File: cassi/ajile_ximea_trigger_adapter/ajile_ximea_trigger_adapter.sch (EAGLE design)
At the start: 10 parts, among them K1 694108105102

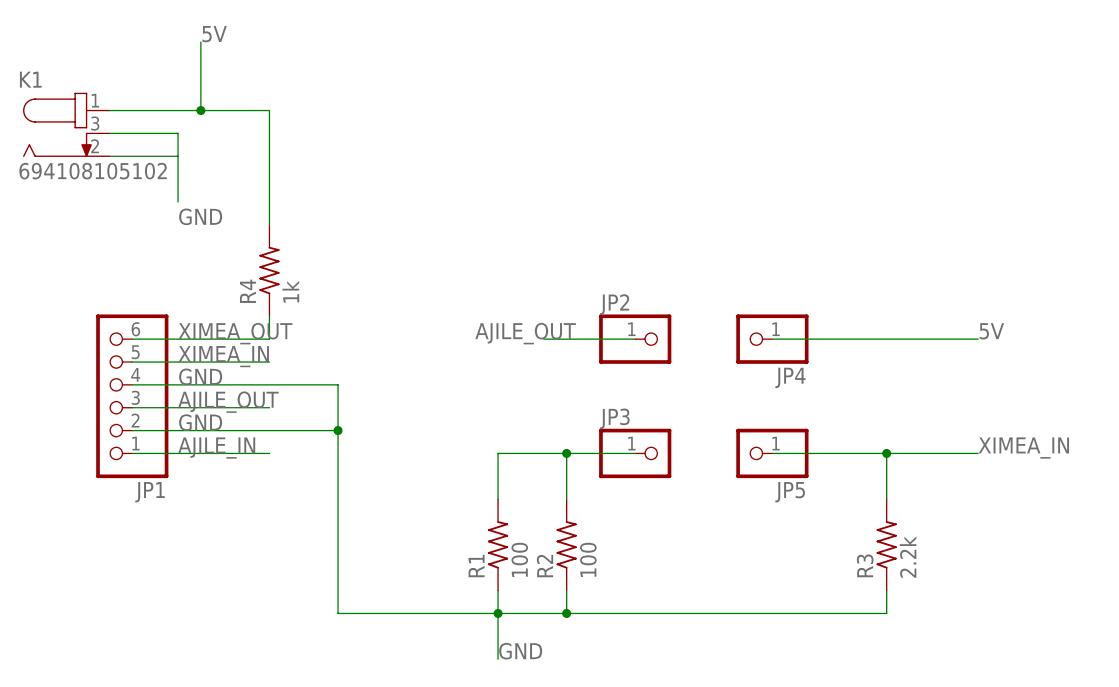
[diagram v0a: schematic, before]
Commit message: finished trigger adapter board
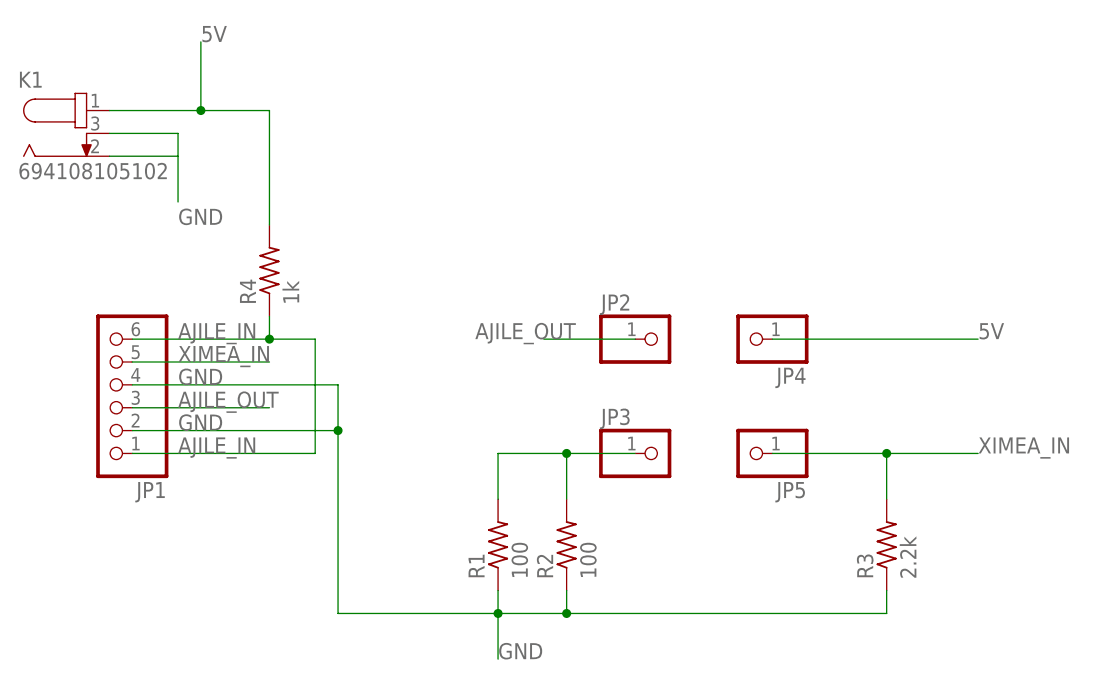
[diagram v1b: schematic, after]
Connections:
- removed net XIMEA_OUT: JP1.6, R4.1
- net AJILE_IN: now also JP1.6, R4.1
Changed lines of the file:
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@@
 </busses>
 <nets>
-<net name="XIMEA_OUT" class="0">
-<segment>
-<pinref part="JP1" gate="A" pin="6"/>
-<wire x1="7.62" y1="45.72" x2="22.86" y2="45.72" width="0.1524" layer="91"/>
-<label x="12.7" y="45.72" size="1.778" layer="95"/>
-<pinref part="R4" gate="G$1" pin="1"/>
-<wire x1="22.86" y1="48.26" x2="22.86" y2="45.72" width="0.1524" layer="91"/>
-</segment>
-</net>
 <net name="XIMEA_IN" class="0">
 <segment>
@@
 <segment>
 <pinref part="JP1" gate="A" pin="1"/>
-<wire x1="7.62" y1="33.02" x2="22.86" y2="33.02" width="0.1524" layer="91"/>
+<wire x1="7.62" y1="33.02" x2="27.94" y2="33.02" width="0.1524" layer="91"/>
 <label x="12.7" y="33.02" size="1.778" layer="95"/>
+<wire x1="27.94" y1="33.02" x2="27.94" y2="45.72" width="0.1524" layer="91"/>
+<pinref part="JP1" gate="A" pin="6"/>
+<wire x1="7.62" y1="45.72" x2="22.86" y2="45.72" width="0.1524" layer="91"/>
+<label x="12.7" y="45.72" size="1.778" layer="95"/>
+<pinref part="R4" gate="G$1" pin="1"/>
+<wire x1="22.86" y1="48.26" x2="22.86" y2="45.72" width="0.1524" layer="91"/>
+<wire x1="27.94" y1="45.72" x2="22.86" y2="45.72" width="0.1524" layer="91"/>
+<junction x="22.86" y="45.72"/>
 </segment>
 </net>
